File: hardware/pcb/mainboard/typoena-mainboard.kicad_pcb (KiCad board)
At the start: 4 copper layers, 130 x 45 mm, 98 parts, among them J1 BATTERIE JST-PH, J10 EXTENSION (non monte), J2 BOUTON contact JST-PH, J3 BOUTON LED JST-PH, J4 FPC 24p 0.5mm - PANNEAU, J5 SECOURS DESPI-C579, J6 USB-C CHARGE + PROG, J7 USB-C CLAVIER (hote), J8 microSD, J9 UART PROG, Q1 AO3401A, Q2 2N7002, Q3 2N7002, Q4 Si1308EDL, Q5 2N7002, Q6 2N7002, SW1 QON, SW2 RESET, SW3 BOOT, U1 ESP32-S3-WROOM-1-N16R8, U2 BQ25896RTW, U3 TPS63001DRCR, U4 TPS61023DRL, U5 CH343P

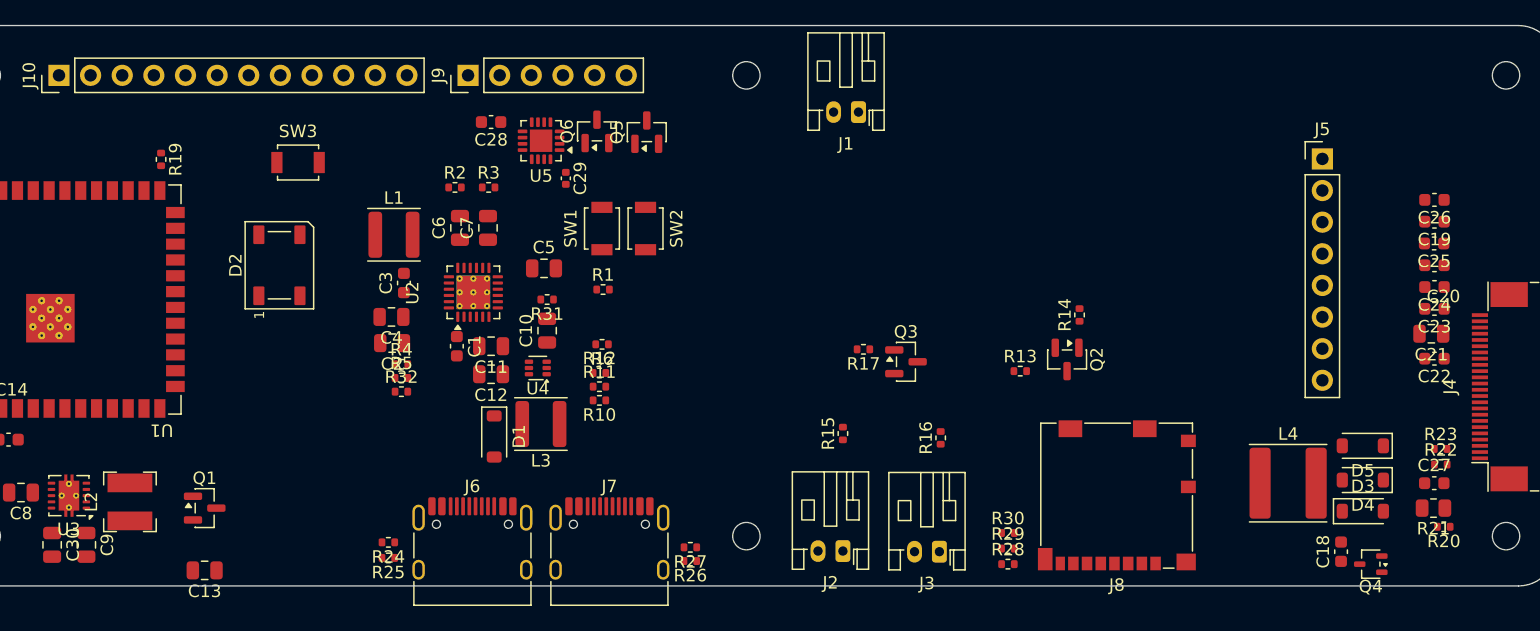
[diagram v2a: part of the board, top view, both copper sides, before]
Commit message: fix(pcb): tighten the pulsed-current loops
Group Q1/Q2/R13/R14/C13 by J8: SD_GATE spans 2.9mm instead of 71, and the
switched rail's only reservoir now sits at the card rather than 72mm away.
Pull C19/C20 against their rectifiers (24->7mm, 15->2mm) and L1 against U2
(6.8->3.2mm).

The panel rail caps move further from J4 as a result. Left as is — 100mm of
FFC behind the connector dominates that path anyway.

Co-Authored-By: Claude Opus 5 <noreply@anthropic.com>
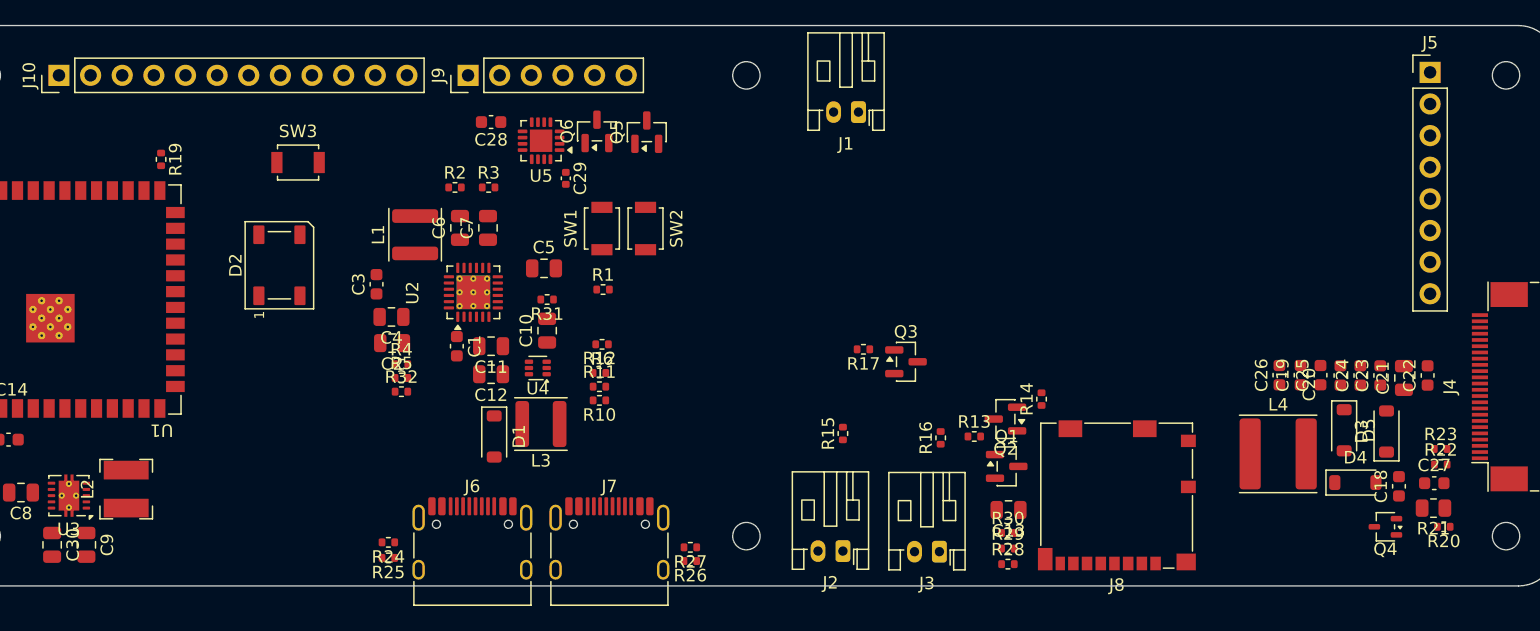
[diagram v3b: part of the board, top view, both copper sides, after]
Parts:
- moved C13 64.7 mm to (126.0, 78.9)
- moved Q1 64.5 mm to (125.9, 75.4)
- moved C26 18.8 mm to (147.8, 68.1), turned to 90 degrees
- moved C19 16.4 mm to (149.5, 68.1), turned to 90 degrees
- moved C25 14.0 mm to (151.1, 68.1), turned to 90 degrees
- moved C20 11.6 mm to (152.7, 68.1), turned to 90 degrees
- moved J5 11.1 mm to (159.9, 43.8)
- moved C24 9.26 mm to (154.3, 68.1), turned to 90 degrees
- moved R14 7.42 mm to (128.7, 70.0)
- moved C18 7.01 mm to (157.4, 77.0)
- moved C23 6.90 mm to (155.9, 68.1), turned to 90 degrees
- moved Q2 6.89 mm to (125.8, 71.6), turned to 180 degrees
- moved D3 6.68 mm to (156.4, 72.6), turned to 90 degrees
- moved R13 6.42 mm to (123.3, 73.0)
- moved C21 4.18 mm to (157.8, 68.3), turned to 90 degrees
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
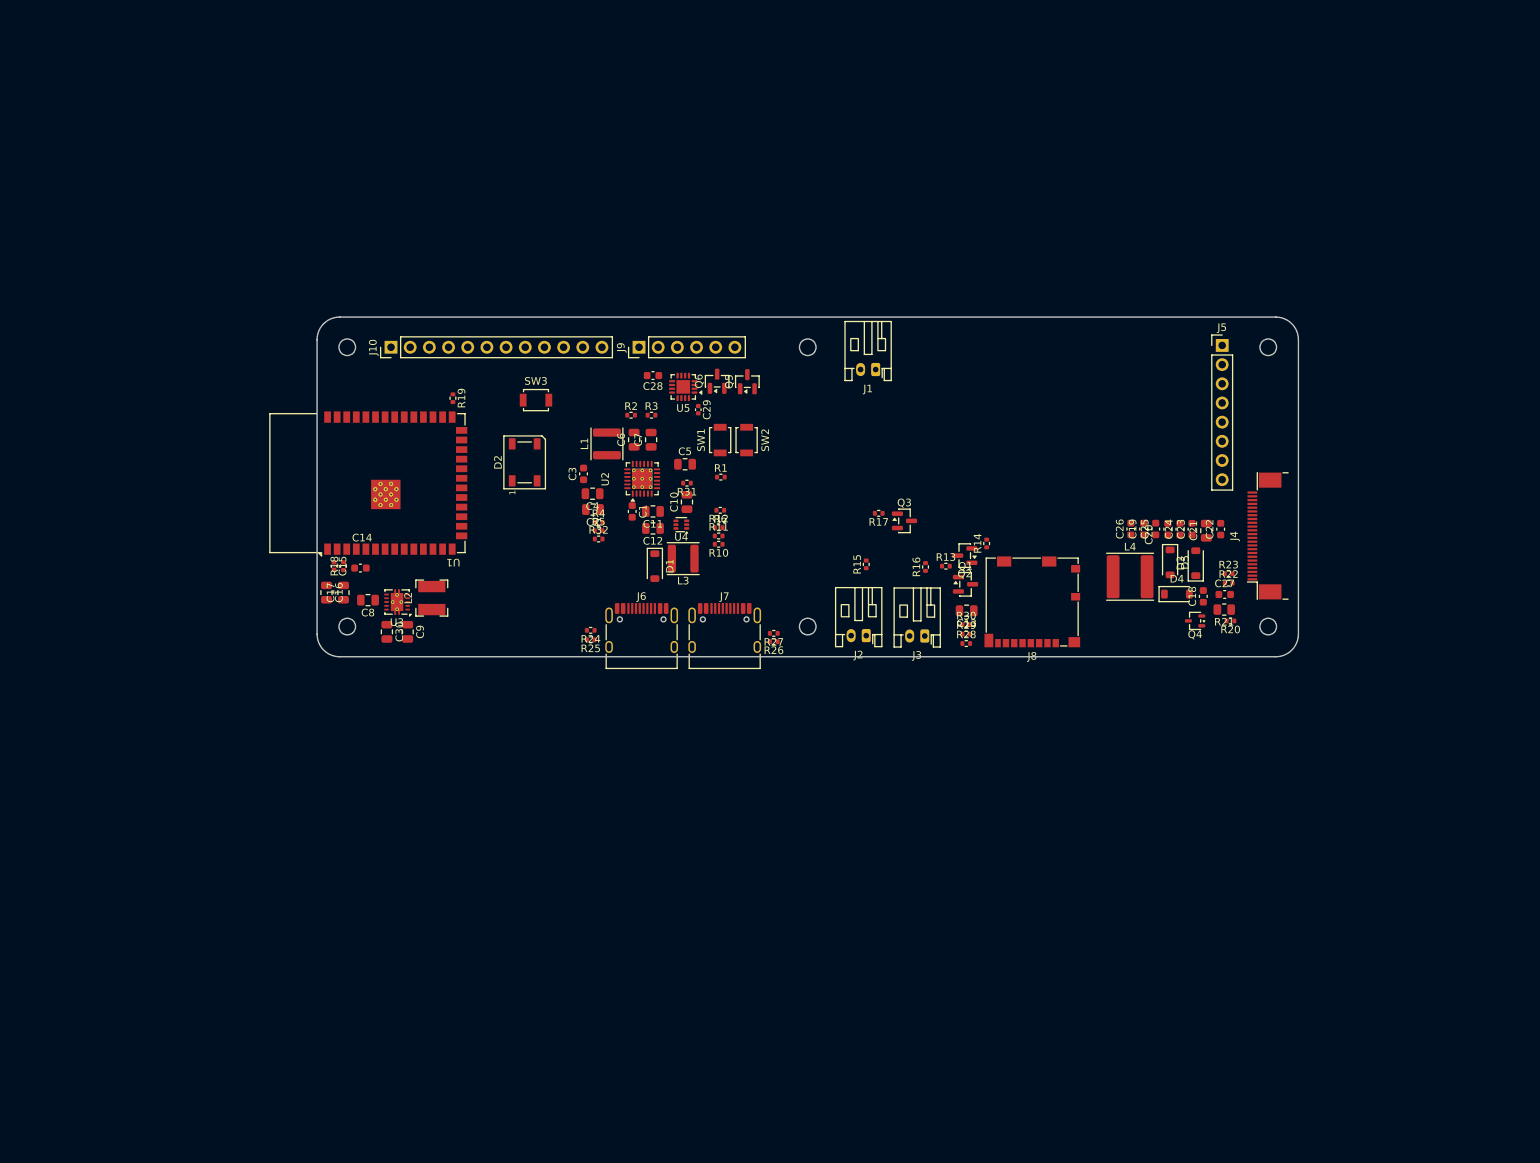
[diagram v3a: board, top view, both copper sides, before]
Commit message: feat(pcb): route the mainboard and add the design checker
801 segments, 110 vias, five filled zones, no unconnected net. Board is
94x45 mm with four #6-32 corner holes; D2 dropped and GPIO 48 exposed on
J10; J4 mechanical pin tied to GND.

tools/check_pcb.py consolidates the checks that were improvised until now:
switching-node discipline, hot loops, decoupling, via-in-pad, fine-pitch
escapes, current capacity, schematic/PCB cross-checks.

Co-Authored-By: Claude Opus 5 <noreply@anthropic.com>
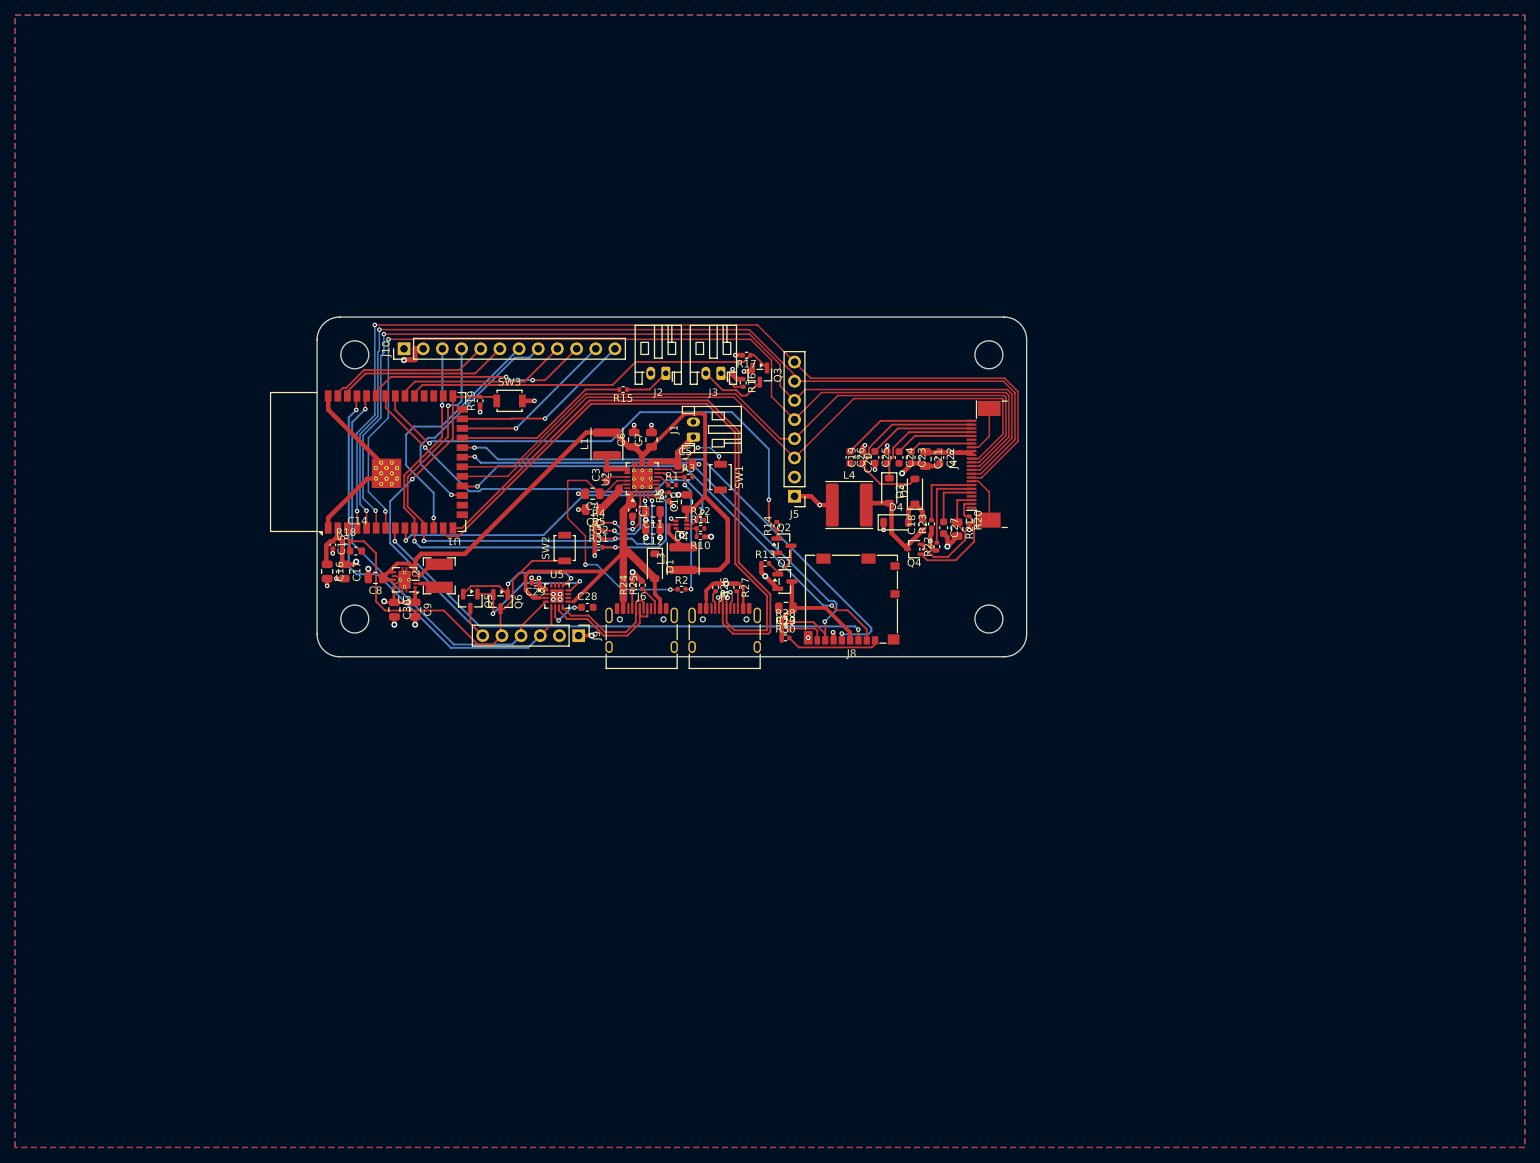
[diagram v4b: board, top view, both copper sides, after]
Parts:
- removed D2: WS2812B, LED_SMD:LED_WS2812B_PLCC4_5.0x5.0mm_P3.2mm
- removed MH5, MH6: MountingHole_2.2mm_M2, MountingHole:MountingHole_2.2mm_M2
- MH1, MH2, MH3, MH4: value MountingHole_2.2mm_M2 -> MountingHole_3.7mm; footprint MountingHole:MountingHole_2.2mm_M2 -> MountingHole:MountingHole_3.7mm
- R10: value 510k -> 510k 1%
- R11: value 68k -> 68k 1%
- moved MH3 126.2 mm to (45.0, 80.0)
- moved MH4 85.0 mm to (129.0, 80.0)
- moved J5 60.1 mm to (103.2, 63.7), turned to 180 degrees
- moved Q5 46.8 mm to (60.3, 77.6), turned to -90 degrees
- moved J3 44.0 mm to (93.5, 47.5)
- moved J2 43.7 mm to (86.2, 47.5)
- moved Q6 40.9 mm to (64.3, 77.7), turned to -90 degrees
- moved R23 39.9 mm to (121.4, 67.4), turned to 90 degrees
- moved R15 39.7 mm to (80.5, 49.6), turned to 180 degrees
- moved J9 39.0 mm to (74.7, 82.2), turned to -90 degrees
- moved R22 39.0 mm to (122.1, 70.4), turned to 90 degrees
- moved C21 38.4 mm to (120.6, 58.8), turned to -90 degrees
- moved C24 38.4 mm to (117.1, 58.6), turned to -90 degrees
- moved C26 38.4 mm to (110.6, 58.6), turned to -90 degrees
- moved C18 38.4 mm to (120.2, 67.5)
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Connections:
- J10 pad 12: GND -> IO48
- J4 pad MP: (no net) -> GND
- U1 pad 25: WS2812_DIN -> IO48
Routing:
- net EPD_BUSY: track 0.00 -> 131.5 mm, vias 0 -> 2
- net EPD_CS: track 0.00 -> 130.1 mm, vias 0 -> 2
- net EPD_DC: track 0.00 -> 129.8 mm, vias 0 -> 2
- net EPD_RST: track 0.00 -> 129.7 mm, vias 0 -> 2
- net VSYS: track 0.00 -> 93.4 mm
- net EPD_MOSI: track 0.00 -> 92.7 mm
- net EPD_SCK: track 0.00 -> 92.0 mm
- net USB_DP: track 0.00 -> 89.3 mm, vias 0 -> 2
- net USB_DM: track 0.00 -> 88.4 mm, vias 0 -> 2
- net GND: track 0.00 -> 82.1 mm, vias 0 -> 34
- net I2C_SDA: track 0.00 -> 71.4 mm, vias 0 -> 4
- net SD_SCK: track 0.00 -> 69.6 mm, vias 0 -> 2
- net SD_MISO: track 0.00 -> 69.5 mm, vias 0 -> 2
- net SD_MOSI: track 0.00 -> 69.5 mm, vias 0 -> 2
- net I2C_SCL: track 0.00 -> 69.2 mm, vias 0 -> 4
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- added copper zone on In2.Cu, net +3V3
- added copper zone on In2.Cu, net +5V
- added copper zone on B.Cu, net GND
- added copper zone on F.Cu, net GND
- added copper zone on In1.Cu, net GND
- added copper zone on In2.Cu, net GND
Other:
- board size 130 x 45 mm -> 94 x 45 mm
